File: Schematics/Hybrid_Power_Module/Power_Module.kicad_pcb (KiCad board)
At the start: 4 copper layers, 69.5 x 60 mm, 135 parts, among them J1 ScrewSwitch, J2 Battery, J3 ScrewSwitch, J4 GSE, J5 USB_C_Female_USB2_Small, J6 SWD_B, J7 Stack Male Edge Connector, Q1 AO4447A, Q2 TSM2309CX, Q3 DMN6040SSD-13, SW1 SW_STM_RESET, SW2 SW_STM_BOOT_MODE, U1 TPS61175PWPR, U10 LM66100DCKR, U11 LM66100DCKR, U12 AMS1117-3.3, U13 CP2102N-A02-GQFN20R, U14 STM32F103CBT6, U15 ISO1044BDR, U16 W25Q128JVS, U2 LM74700QDBVRQ1, U3 LM74700QDBVRQ1, U4 ACS37041KLHBLT-010B3, U5 ACS37041KLHBLT-010B5, U6 INA181A2, U7 LMR51430XDDCR, U8 LMR51430XDDCR, U9 LM66100DCKR, Y1 X322516MMB4SI

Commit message: fix part number and bom formation, update mostfet based on stock
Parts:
- D7: value 24V PWR (YLW) -> 24V PWR (WHIT)
- Q2: value TSM2309CX -> SI2305CDS

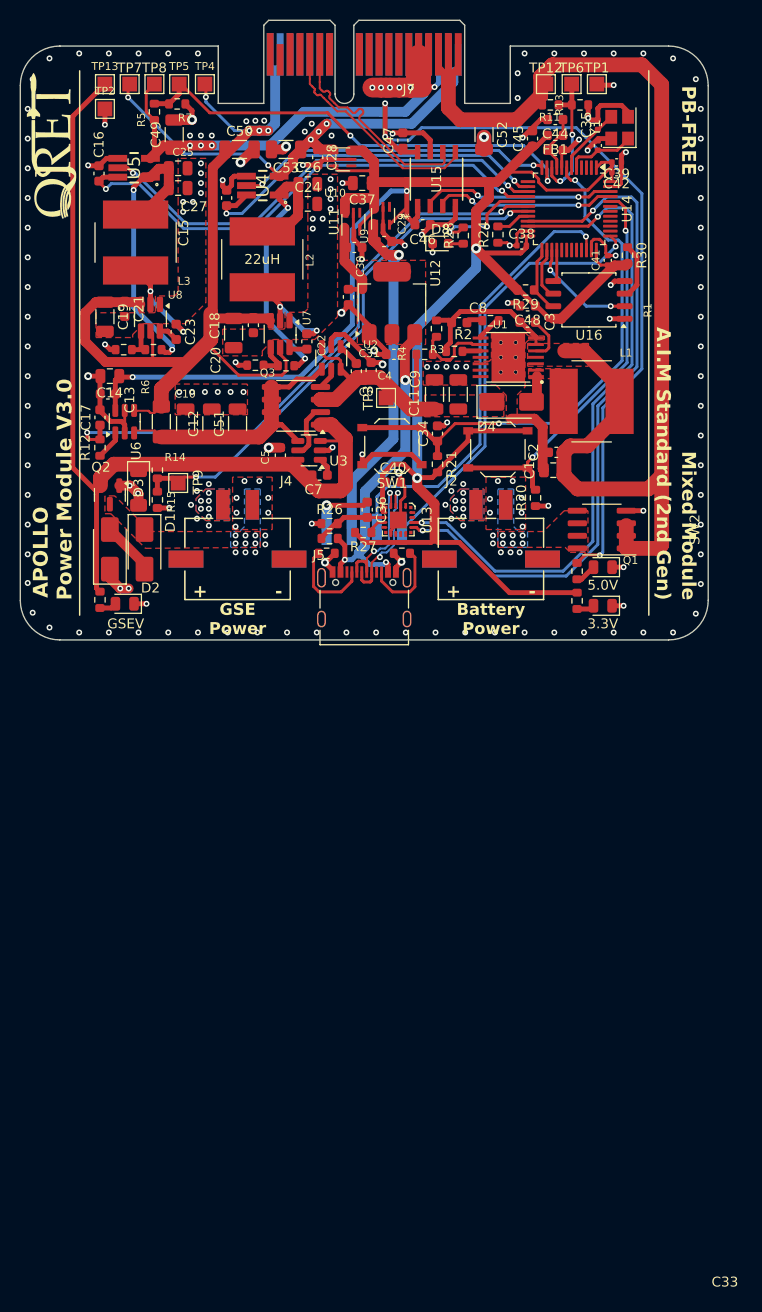
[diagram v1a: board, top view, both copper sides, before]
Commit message: finished power board silkscreen, needs final review before approval
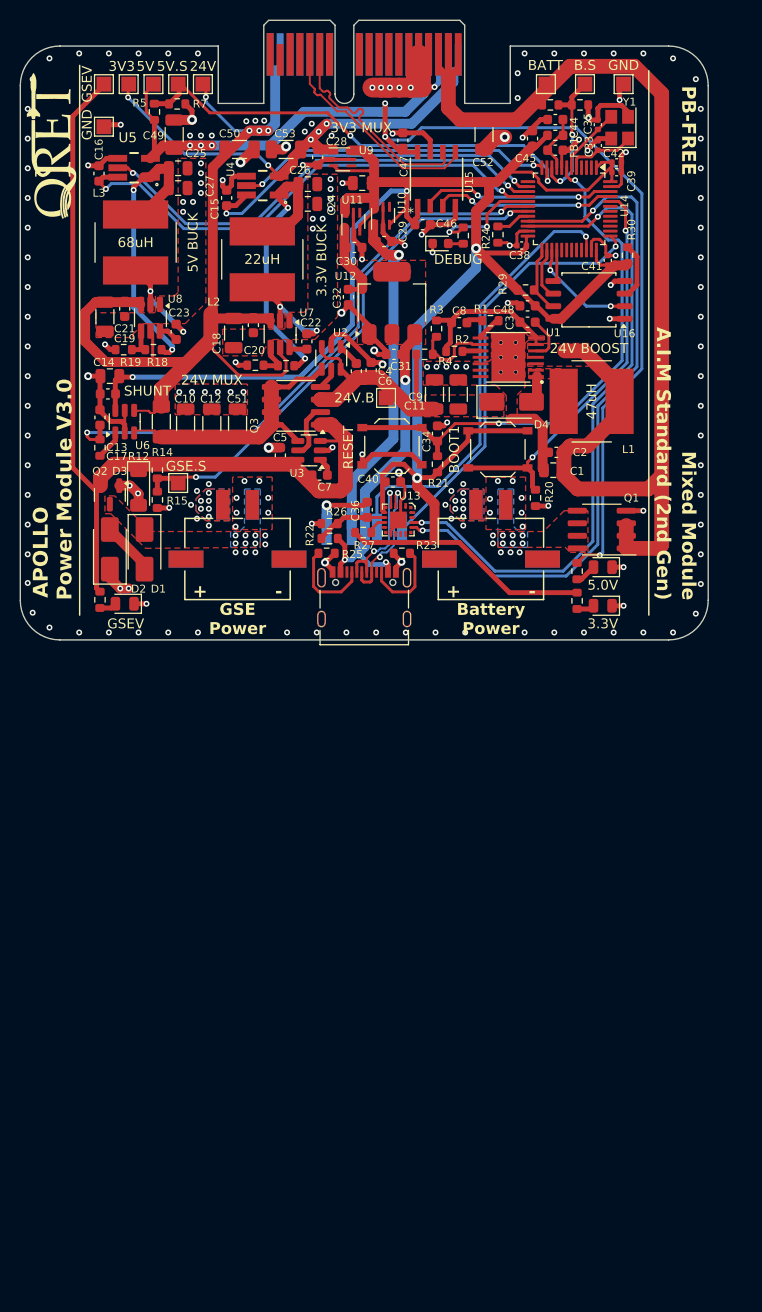
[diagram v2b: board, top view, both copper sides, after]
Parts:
- moved TP1 2.70 mm to (191.2, 43.6)
- moved TP2 1.80 mm to (138.7, 47.9)
- moved TP6 1.35 mm to (187.3, 43.6)
- moved TP4 0.20 mm to (148.7, 43.6)
- moved TP13 0.10 mm to (138.7, 43.6)
- moved TP5 0.10 mm to (146.2, 43.6)
- moved TP7 0.10 mm to (141.2, 43.6)
- moved TP8 0.10 mm to (143.7, 43.6)
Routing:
- net V_BATT: track 114.7 -> 112.9 mm
- net GND: track 214.5 -> 215.3 mm, vias 198 -> 195
- net BATT_SENSE: track 13.7 -> 14.2 mm

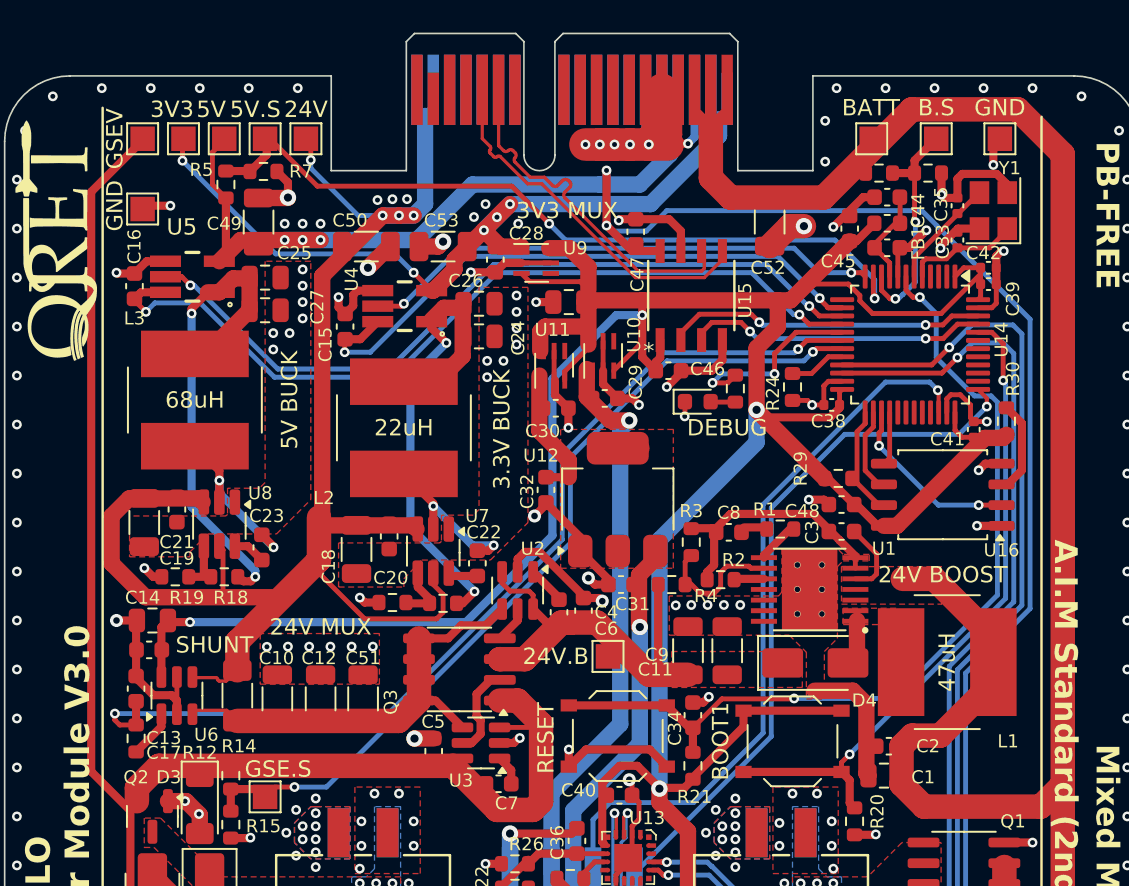
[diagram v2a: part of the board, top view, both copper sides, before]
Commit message: minor updates to part numbers and silkscreen
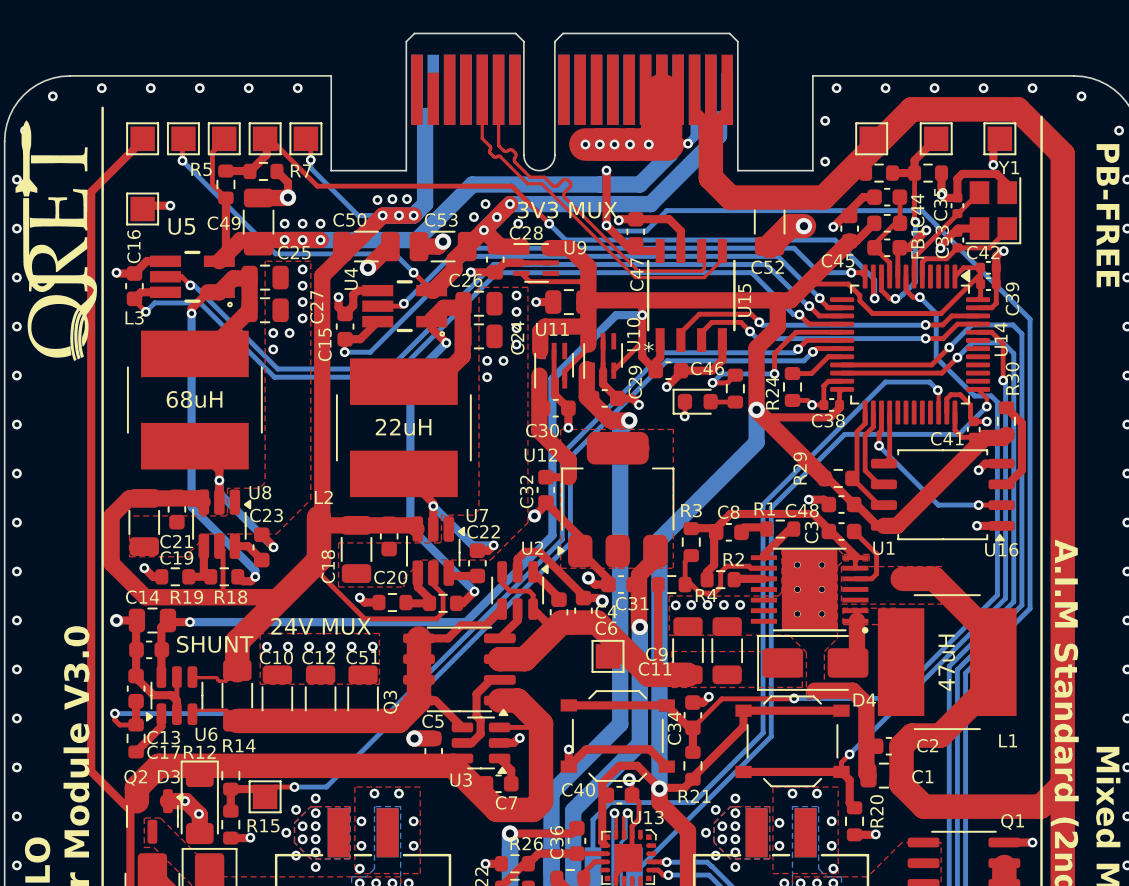
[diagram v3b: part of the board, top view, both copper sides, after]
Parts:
- FB1: value 100R -> 600R
- R10: value 12K -> 12k
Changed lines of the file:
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@@
 			)
 		)
-		(property "Description" "GND"
+		(property "Description" ""
 			(at 0 -1.9 0)
 			(unlocked yes)
@@
 			)
 		)
-		(property "Description" "3V3"
+		(property "Description" ""
 			(at -0.7 -1.8 0)
 			(unlocked yes)
@@
 			)
 		)
-		(property "Description" "5V BUCK"
+		(property "Description" ""
 			(at -7.6 -4.3 90)
 			(unlocked yes)
@@
 			)
 		)
-		(property "Description" "GSEV"
+		(property "Description" ""
 			(at -1.7 0 90)
 			(unlocked yes)
@@
 			)
 		)
-		(property "Description" "3.3V BUCK"
+		(property "Description" ""
 			(at -7.45 -4.2 90)
 			(unlocked yes)
@@
 		(at 168.435 87.635 -90)
 		(property "Reference" "U13"
-			(at -2.435 -1.165 360)
+			(at -2.435 -1.165 0)
 			(layer "F.SilkS")
 			(effects
@@
 			)
 		)
-		(property "Description" "B.S"
+		(property "Description" ""
 			(at 0 -1.9 0)
 			(unlocked yes)
@@
 			)
 		)
-		(property "Value" "100R"
+		(property "Value" "600R"
 			(at 0 1.43 0)
 			(layer "F.Fab")
@@
 			)
 		)
-		(property "Description" "24V"
+		(property "Description" ""
 			(at 0 -1.8 0)
 			(unlocked yes)
@@
 			)
 		)
-		(property "Description" "DEBUG"
+		(property "Description" ""
 			(at 1.8 1.6 0)
 			(unlocked yes)
@@
 			)
 		)
-		(property "LCSC" "C72038"
+		(property "LCSC" "C2290"
 			(at 0 0 0)
 			(unlocked yes)
@@
 			)
 		)
-		(property "Description" "5V"
+		(property "Description" ""
 			(at -0.8 -1.8 0)
 			(unlocked yes)
@@
 			)
 		)
-		(property "Description" "BATT"
+		(property "Description" ""
 			(at -0.05 -1.9 0)
 			(unlocked yes)
@@
 			)
 		)
-		(property "Description" "GND"
+		(property "Description" ""
 			(at -1.7 -0.2 90)
 			(unlocked yes)
@@
 			)
 		)
-		(property "Value" "12K"
+		(property "Value" "12k"
 			(at 0 1.43 90)
 			(layer "F.Fab")
@@
 			)
 		)
-		(property "Description" "24V.B"
+		(property "Description" ""
 			(at 0 -3.2 0)
 			(unlocked yes)
@@
 			)
 		)
-		(property "Description" "24V BOOST"
+		(property "Description" ""
 			(at -8.15 0.9 0)
 			(layer "F.SilkS" knockout)
@@
 			)
 		)
-		(property "Description" "5V.S"
+		(property "Description" ""
 			(at -0.6 -1.8 0)
 			(unlocked yes)
@@
 			)
 		)
-		(property "Description" "GSE.S"
+		(property "Description" ""
 			(at -0.8 1.7 0)
 			(unlocked yes)
@@
 			)
 		)
-		(property "Description" "BOOT1"
+		(property "Description" ""
 			(at 4.4 0 90)
 			(unlocked yes)
@@
 			)
 		)
-		(property "Description" "RESET"
+		(property "Description" ""
 			(at 4.4 -0.125 90)
 			(unlocked yes)

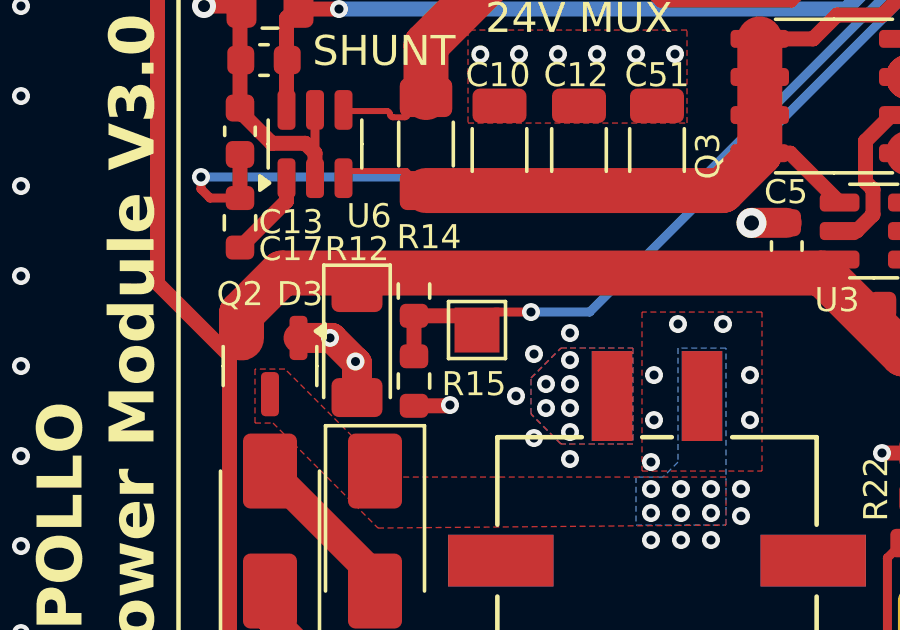
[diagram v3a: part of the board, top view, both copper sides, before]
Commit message: fixed voltage divder for GSE 24v
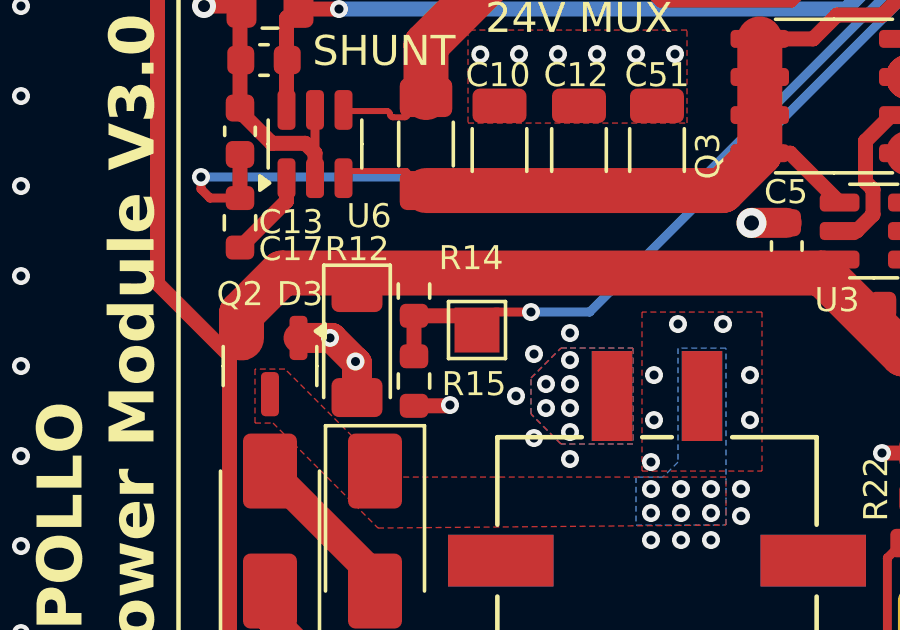
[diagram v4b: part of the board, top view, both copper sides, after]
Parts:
- R14: value 10k -> 100k
- R15: value 100k -> 10k
- turned R14 to -90 degrees
- turned R15 to 90 degrees
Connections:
- R14 pad 1: GSE_SENSE -> 24V_GSE
- R14 pad 2: 24V_GSE -> GSE_SENSE
- R15 pad 1: GSE_SENSE -> GND
- R15 pad 2: GND -> GSE_SENSE
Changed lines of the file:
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@@
 	(footprint "Resistor_SMD:R_0603_1608Metric"
 		(layer "F.Cu")
-		(at 144.1 82.6 90)
+		(at 144.1 82.6 -90)
 		(descr "Resistor SMD 0603 (1608 Metric), square (rectangular) end terminal, IPC_7351 nominal, (Body size source: IPC-SM-782 page 72, https://www.pcb-3d.com/wordpress/wp-content/uploads/ipc-sm-782a_amendment_1_and_2.pdf), generated with kicad-footprint-generator")
 		(tags "resistor")
 		(property "Reference" "R14"
-			(at 1.8 0.5 180)
+			(at -1.1 -1.9 360)
 			(layer "F.SilkS")
 			(effects
@@
 			)
 		)
-		(property "Value" "10k"
+		(property "Value" "100k"
 			(at 0 1.43 90)
 			(layer "F.Fab")
@@
 			)
 		)
-		(property "Description" ""
-			(at 0 0 90)
-			(layer "F.Fab")
-			(hide yes)
-			(effects
-				(font
-					(size 1.27 1.27)
-					(thickness 0.15)
-				)
-			)
-		)
-		(property "LCSC" "C25804"
-			(at 101.5 241.9 0)
+		(property "Description" "Resistor"
+			(at 0 0 90)
+			(layer "F.Fab")
+			(hide yes)
+			(effects
+				(font
+					(size 1.27 1.27)
+					(thickness 0.15)
+				)
+			)
+		)
+		(property "LCSC" "C25803"
+			(at 101.5 241.9 360)
 			(layer "F.Fab")
 			(hide yes)
@@
 		(attr smd)
 		(fp_line
+			(start -0.237258 0.5225)
+			(end 0.237258 0.5225)
+			(stroke
+				(width 0.12)
+				(type solid)
+			)
+			(layer "F.SilkS")
+		)
+		(fp_line
 			(start -0.237258 -0.5225)
 			(end 0.237258 -0.5225)
@@
 		)
 		(fp_line
-			(start -0.237258 0.5225)
-			(end 0.237258 0.5225)
-			(stroke
-				(width 0.12)
-				(type solid)
-			)
-			(layer "F.SilkS")
+			(start -1.48 0.73)
+			(end -1.48 -0.73)
+			(stroke
+				(width 0.05)
+				(type solid)
+			)
+			(layer "F.CrtYd")
+		)
+		(fp_line
+			(start 1.48 0.73)
+			(end -1.48 0.73)
+			(stroke
+				(width 0.05)
+				(type solid)
+			)
+			(layer "F.CrtYd")
+		)
+		(fp_line
+			(start -1.48 -0.73)
+			(end 1.48 -0.73)
+			(stroke
+				(width 0.05)
+				(type solid)
+			)
+			(layer "F.CrtYd")
 		)
 		(fp_line
@@
 		)
 		(fp_line
-			(start -1.48 -0.73)
-			(end 1.48 -0.73)
-			(stroke
-				(width 0.05)
-				(type solid)
-			)
-			(layer "F.CrtYd")
-		)
-		(fp_line
-			(start 1.48 0.73)
-			(end -1.48 0.73)
-			(stroke
-				(width 0.05)
-				(type solid)
-			)
-			(layer "F.CrtYd")
-		)
-		(fp_line
-			(start -1.48 0.73)
-			(end -1.48 -0.73)
-			(stroke
-				(width 0.05)
-				(type solid)
-			)
-			(layer "F.CrtYd")
+			(start -0.8 0.4125)
+			(end -0.8 -0.4125)
+			(stroke
+				(width 0.1)
+				(type solid)
+			)
+			(layer "F.Fab")
+		)
+		(fp_line
+			(start 0.8 0.4125)
+			(end -0.8 0.4125)
+			(stroke
+				(width 0.1)
+				(type solid)
+			)
+			(layer "F.Fab")
+		)
+		(fp_line
+			(start -0.8 -0.4125)
+			(end 0.8 -0.4125)
+			(stroke
+				(width 0.1)
+				(type solid)
+			)
+			(layer "F.Fab")
 		)
 		(fp_line
@@
 			(layer "F.Fab")
 		)
-		(fp_line
-			(start -0.8 -0.4125)
-			(end 0.8 -0.4125)
-			(stroke
-				(width 0.1)
-				(type solid)
-			)
-			(layer "F.Fab")
-		)
-		(fp_line
-			(start 0.8 0.4125)
-			(end -0.8 0.4125)
-			(stroke
-				(width 0.1)
-				(type solid)
-			)
-			(layer "F.Fab")
-		)
-		(fp_line
-			(start -0.8 0.4125)
-			(end -0.8 -0.4125)
-			(stroke
-				(width 0.1)
-				(type solid)
-			)
-			(layer "F.Fab")
-		)
 		(fp_text user "${REFERENCE}"
 			(at 0 0 90)
@@
 		)
 		(pad "1" smd roundrect
-			(at -0.825 0 90)
+			(at -0.825 0 270)
+			(size 0.8 0.95)
+			(layers "F.Cu" "F.Paste" "F.Mask")
+			(roundrect_rratio 0.25)
+			(net 19 "24V_GSE")
+			(pintype "passive")
+		)
+		(pad "2" smd roundrect
+			(at 0.825 0 270)
 			(size 0.8 0.95)
 			(layers "F.Cu" "F.Paste" "F.Mask")
 			(roundrect_rratio 0.25)
 			(net 58 "GSE_SENSE")
-			(pintype "passive")
-		)
-		(pad "2" smd roundrect
-			(at 0.825 0 90)
-			(size 0.8 0.95)
-			(layers "F.Cu" "F.Paste" "F.Mask")
-			(roundrect_rratio 0.25)
-			(net 19 "24V_GSE")
 			(pintype "passive")
 		)
@@
 	(footprint "Resistor_SMD:R_0603_1608Metric"
 		(layer "F.Cu")
-		(at 144.1 85.6 -90)
+		(at 144.1 85.6 90)
 		(descr "Resistor SMD 0603 (1608 Metric), square (rectangular) end terminal, IPC_7351 nominal, (Body size source: IPC-SM-782 page 72, https://www.pcb-3d.com/wordpress/wp-content/uploads/ipc-sm-782a_amendment_1_and_2.pdf), generated with kicad-footprint-generator")
 		(tags "resistor")
 		(property "Reference" "R15"
-			(at 0.1 -2 180)
+			(at -0.1 2 360)
 			(layer "F.SilkS")
 			(effects
@@
 			)
 		)
-		(property "Value" "100k"
+		(property "Value" "10k"
 			(at 0 1.43 90)
 			(layer "F.Fab")
@@
 			)
 		)
-		(property "Description" "Resistor"
-			(at 0 0 90)
-			(layer "F.Fab")
-			(hide yes)
-			(effects
-				(font
-					(size 1.27 1.27)
-					(thickness 0.15)
-				)
-			)
-		)
-		(property "LCSC" "C25803"
-			(at 98.1 245.3 0)
+		(property "Description" ""
+			(at 0 0 90)
+			(layer "F.Fab")
+			(hide yes)
+			(effects
+				(font
+					(size 1.27 1.27)
+					(thickness 0.15)
+				)
+			)
+		)
+		(property "LCSC" "C25804"
+			(at 98.1 245.3 360)
 			(layer "F.Fab")
 			(hide yes)
@@
 		(attr smd)
 		(fp_line
+			(start -0.237258 -0.5225)
+			(end 0.237258 -0.5225)
+			(stroke
+				(width 0.12)
+				(type solid)
+			)
+			(layer "F.SilkS")
+		)
+		(fp_line
 			(start -0.237258 0.5225)
 			(end 0.237258 0.5225)
@@
 		)
 		(fp_line
-			(start -0.237258 -0.5225)
-			(end 0.237258 -0.5225)
-			(stroke
-				(width 0.12)
-				(type solid)
-			)
-			(layer "F.SilkS")
+			(start 1.48 -0.73)
+			(end 1.48 0.73)
+			(stroke
+				(width 0.05)
+				(type solid)
+			)
+			(layer "F.CrtYd")
+		)
+		(fp_line
+			(start -1.48 -0.73)
+			(end 1.48 -0.73)
+			(stroke
+				(width 0.05)
+				(type solid)
+			)
+			(layer "F.CrtYd")
+		)
+		(fp_line
+			(start 1.48 0.73)
+			(end -1.48 0.73)
+			(stroke
+				(width 0.05)
+				(type solid)
+			)
+			(layer "F.CrtYd")
 		)
 		(fp_line
@@
 		)
 		(fp_line
-			(start 1.48 0.73)
-			(end -1.48 0.73)
-			(stroke
-				(width 0.05)
-				(type solid)
-			)
-			(layer "F.CrtYd")
-		)
-		(fp_line
-			(start -1.48 -0.73)
-			(end 1.48 -0.73)
-			(stroke
-				(width 0.05)
-				(type solid)
-			)
-			(layer "F.CrtYd")
-		)
-		(fp_line
-			(start 1.48 -0.73)
-			(end 1.48 0.73)
-			(stroke
-				(width 0.05)
-				(type solid)
-			)
-			(layer "F.CrtYd")
+			(start 0.8 -0.4125)
+			(end 0.8 0.4125)
+			(stroke
+				(width 0.1)
+				(type solid)
+			)
+			(layer "F.Fab")
+		)
+		(fp_line
+			(start -0.8 -0.4125)
+			(end 0.8 -0.4125)
+			(stroke
+				(width 0.1)
+				(type solid)
+			)
+			(layer "F.Fab")
+		)
+		(fp_line
+			(start 0.8 0.4125)
+			(end -0.8 0.4125)
+			(stroke
+				(width 0.1)
+				(type solid)
+			)
+			(layer "F.Fab")
 		)
 		(fp_line
@@
 			(layer "F.Fab")
 		)
-		(fp_line
-			(start 0.8 0.4125)
-			(end -0.8 0.4125)
-			(stroke
-				(width 0.1)
-				(type solid)
-			)
-			(layer "F.Fab")
-		)
-		(fp_line
-			(start -0.8 -0.4125)
-			(end 0.8 -0.4125)
-			(stroke
-				(width 0.1)
-				(type solid)
-			)
-			(layer "F.Fab")
-		)
-		(fp_line
-			(start 0.8 -0.4125)
-			(end 0.8 0.4125)
-			(stroke
-				(width 0.1)
-				(type solid)
-			)
-			(layer "F.Fab")
-		)
 		(fp_text user "${REFERENCE}"
 			(at 0 0 90)
@@
 		)
 		(pad "1" smd roundrect
-			(at -0.825 0 270)
+			(at -0.825 0 90)
+			(size 0.8 0.95)
+			(layers "F.Cu" "F.Paste" "F.Mask")
+			(roundrect_rratio 0.25)
+			(net 1 "GND")
+			(pintype "passive")
+		)
+		(pad "2" smd roundrect
+			(at 0.825 0 90)
 			(size 0.8 0.95)
 			(layers "F.Cu" "F.Paste" "F.Mask")
@@
 			(pintype "passive")
 		)
-		(pad "2" smd roundrect
-			(at 0.825 0 270)
-			(size 0.8 0.95)
-			(layers "F.Cu" "F.Paste" "F.Mask")
-			(roundrect_rratio 0.25)
-			(net 1 "GND")
-			(pintype "passive")
-		)
